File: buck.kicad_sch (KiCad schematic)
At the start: 24 parts, among them IC2 LV2862YDDCR, IC2 RT6285GSP

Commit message: Update footprints + pass DRC
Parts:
- L1: footprint Robomaster_ICs:MPLAL6060100 -> Robomaster_Passives:MPLAL6060100
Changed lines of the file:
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@@
       (effects (font (size 1.27 1.27)))
     )
-    (property "Footprint" "Robomaster_ICs:MPLAL6060100" (at 114.3 90.17 0)
+    (property "Footprint" "Robomaster_Passives:MPLAL6060100" (at 114.3 90.17 0)
       (effects (font (size 1.27 1.27)) hide)
     )

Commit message: Replace inductor with larger
Idk how much current it'll need + invalid inductor data for spreadsheet
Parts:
- L1: footprint Inductor_SMD:L_Murata_LQH2MCNxxxx02_2.0x1.6mm -> Robomaster_Passives:SRN3012BTA330M; Manufacturer_Name (none) -> Bourns; Manufacturer_Part_Number (none) -> SRN3012BTA-330M; Mouser Part Number (none) -> 652-SRN3012BTA-330M
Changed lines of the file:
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@@
       (effects (font (size 1.27 1.27)))
     )
-    (property "Footprint" "Inductor_SMD:L_Murata_LQH2MCNxxxx02_2.0x1.6mm" (at 139.7 130.81 0)
+    (property "Footprint" "Robomaster_Passives:SRN3012BTA330M" (at 139.7 130.81 0)
       (effects (font (size 1.27 1.27)) hide)
     )
-    (property "Datasheet" "https://www.we-online.com/components/products/datasheet/74404024330.pdf" (at 139.7 130.81 0)
+    (property "Datasheet" "https://www.mouser.com/datasheet/2/54/Bourns_08042023_SRN3012BTA_datasheet-3305898.pdf" (at 139.7 130.81 0)
       (effects (font (size 1.27 1.27)) hide)
     )
+    (property "Manufacturer_Name" "Bourns" (at 139.7 130.81 0)
+      (effects (font (size 1.27 1.27)) hide)
+    )
+    (property "Manufacturer_Part_Number" "SRN3012BTA-330M" (at 139.7 130.81 0)
+      (effects (font (size 1.27 1.27)) hide)
+    )
+    (property "Mouser Part Number" "652-SRN3012BTA-330M" (at 139.7 130.81 0)
+      (effects (font (size 1.27 1.27)) hide)
+    )

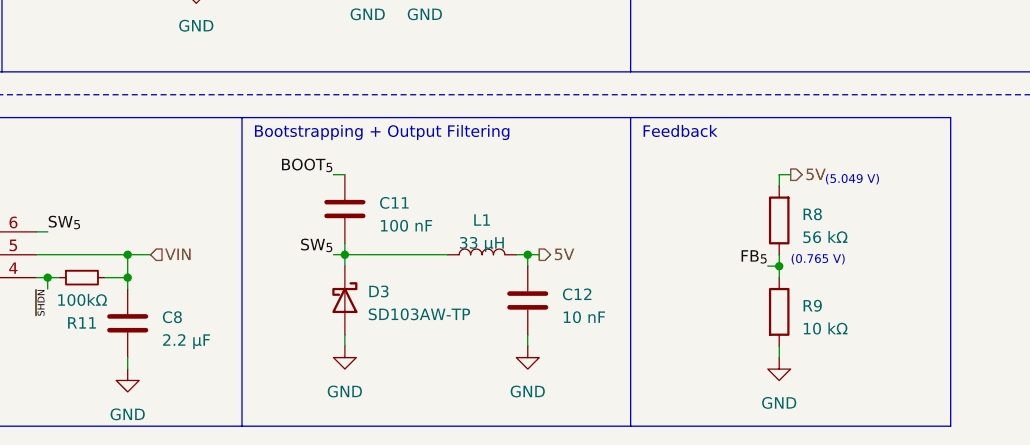
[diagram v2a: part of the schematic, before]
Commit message: Update and generate IBOM
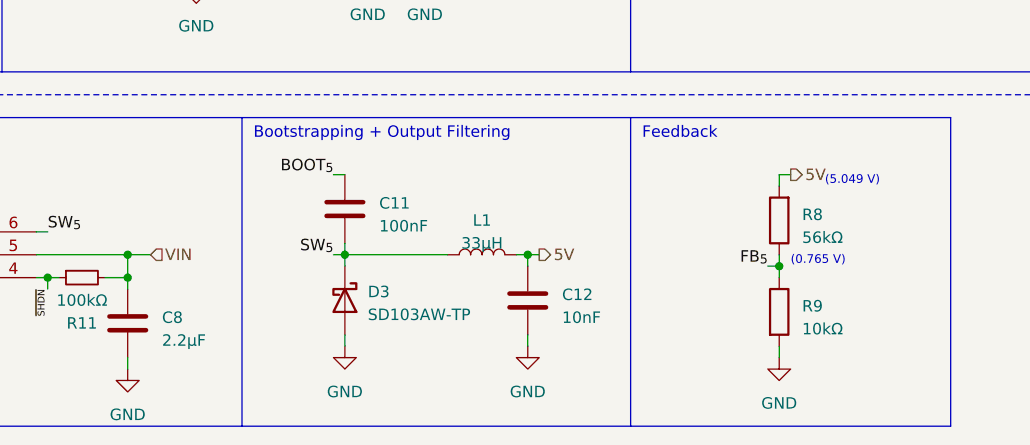
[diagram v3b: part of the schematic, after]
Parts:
- C1: Manufacturer_Part_Number (none) -> C0603C103J5RACAUTO; Mouser Part Number (none) -> 80-C0603C103J5RAUTO
- C11: value 100 nF -> 100nF; Manufacturer_Part_Number (none) -> CL10B104JB8NNNC; Mouser Part Number (none) -> 187-CL10B104JB8NNNC
- C12: value 10 nF -> 10nF; Manufacturer_Part_Number (none) -> C0603C103J5RACAUTO; Mouser Part Number (none) -> 80-C0603C103J5RAUTO
- C3: Manufacturer_Part_Number (none) -> CC0603FRNPO0BN820; Mouser Part Number (none) -> 603-CC0603FRNP0BN820
- C5, C6: Manufacturer_Part_Number (none) -> CL21A226MAYNNNE; Mouser Part Number (none) -> 187-CL21A226MAYNNNE
- C7, C8: Manufacturer_Part_Number (none) -> C1608X5R1E475K080AC; Mouser Part Number (none) -> 810-C1608X5R1E475K
- C8: value 2.2 μF -> 2.2μF; Manufacturer_Part_Number (none) -> GRM188R61E225KA2J; Mouser Part Number (none) -> 81-GRM188R61E225KA2J
- D3: Manufacturer_Part_Number (none) -> BAS321JX; Mouser Part Number (none) -> 771-BAS321JX
- D3: Manufacturer_Part_Number (none) -> SD103AW-TP; Mouser Part Number (none) -> 833-SD103AW-TP
- D4: Manufacturer_Part_Number (none) -> SR54F-AU_R2_000A1; Mouser Part Number (none) -> 241-SR54F-AUR1000A1
- L1: Manufacturer_Part_Number (none) -> MPL-AL6060-100; Mouser Part Number (none) -> 946-MPL-AL6060-100
- L1: value 33 μH -> 33μH
- R11, R3: Manufacturer_Part_Number (none) -> RT0603DRE07100KL; Mouser Part Number (none) -> 603-RT0603DRE07100KL
- R4: Manufacturer_Part_Number (none) -> RT0603DRE076K8L; Mouser Part Number (none) -> 603-RT0603DRE076K8L
- R8: value 56 kΩ -> 56kΩ; Manufacturer_Part_Number (none) -> RT0603DRD0756KL; Mouser Part Number (none) -> 603-RT0603DRD0756KL
- R9: value 10 kΩ -> 10kΩ; Manufacturer_Part_Number (none) -> RT0603DRE0710KL; Mouser Part Number (none) -> 603-RT0603DRE0710KL
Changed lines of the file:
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@@
+      (effects (font (size 1.27 1.27)) hide)
+    )
+    (property "Manufacturer_Part_Number" "C1608X5R1E475K080AC" (at 142.24 60.96 0)
+      (effects (font (size 1.27 1.27)) hide)
+    )
+    (property "Mouser Part Number" "810-C1608X5R1E475K" (at 142.24 60.96 0)
       (effects (font (size 1.27 1.27)) hide)
     )
@@
       (effects (font (size 1.27 1.27)) hide)
     )
+    (property "Manufacturer_Part_Number" "CC0603FRNPO0BN820" (at 110.49 55.88 0)
+      (effects (font (size 1.27 1.27)) hide)
+    )
+    (property "Mouser Part Number" "603-CC0603FRNP0BN820" (at 110.49 55.88 0)
+      (effects (font (size 1.27 1.27)) hide)
+    )
     (pin "1")
     (pin "2")
@@
     )
     (property "Datasheet" "~" (at 97.79 66.04 0)
+      (effects (font (size 1.27 1.27)) hide)
+    )
+    (property "Manufacturer_Part_Number" "RT0603DRE076K8L" (at 97.79 66.04 0)
+      (effects (font (size 1.27 1.27)) hide)
+    )
+    (property "Mouser Part Number" "603-RT0603DRE076K8L" (at 97.79 66.04 0)
       (effects (font (size 1.27 1.27)) hide)
     )
@@
       (effects (font (size 1.27 1.27)) hide)
     )
+    (property "Manufacturer_Part_Number" "SR54F-AU_R2_000A1" (at 107.95 95.25 0)
+      (effects (font (size 1.27 1.27)) hide)
+    )
+    (property "Mouser Part Number" "241-SR54F-AUR1000A1" (at 107.95 95.25 0)
+      (effects (font (size 1.27 1.27)) hide)
+    )
     (pin "1")
     (pin "2")
@@
     )
     (property "Datasheet" "https://www.mouser.com/datasheet/2/277/MPL_AL6060_100-2946374.pdf" (at 114.3 90.17 0)
+      (effects (font (size 1.27 1.27)) hide)
+    )
+    (property "Manufacturer_Part_Number" "MPL-AL6060-100" (at 114.3 90.17 0)
+      (effects (font (size 1.27 1.27)) hide)
+    )
+    (property "Mouser Part Number" "946-MPL-AL6060-100" (at 114.3 90.17 0)
       (effects (font (size 1.27 1.27)) hide)
     )
@@
       (effects (font (size 1.27 1.27)) hide)
     )
-    (property "Datasheet" "https://www.mouser.com/datasheet/2/447/KEM_C1002_X7R_SMD-3316098.pdf" (at 71.12 83.82 0)
+    (property "Datasheet" "~" (at 71.12 83.82 0)
+      (effects (font (size 1.27 1.27)) hide)
+    )
+    (property "Manufacturer_Part_Number" "C0603C103J5RACAUTO" (at 71.12 83.82 0)
+      (effects (font (size 1.27 1.27)) hide)
+    )
+    (property "Mouser Part Number" "80-C0603C103J5RAUTO" (at 71.12 83.82 0)
       (effects (font (size 1.27 1.27)) hide)
     )
@@
       (effects (font (size 1.27 1.27)) (justify right))
     )
-    (property "Value" "56 kΩ" (at 175.26 128.905 0)
+    (property "Value" "56kΩ" (at 175.26 128.905 0)
       (effects (font (size 1.27 1.27)) (justify right))
     )
@@
     )
     (property "Datasheet" "~" (at 172.72 127 0)
+      (effects (font (size 1.27 1.27)) hide)
+    )
+    (property "Manufacturer_Part_Number" "RT0603DRD0756KL" (at 172.72 127 0)
+      (effects (font (size 1.27 1.27)) hide)
+    )
+    (property "Mouser Part Number" "603-RT0603DRD0756KL" (at 172.72 127 0)
       (effects (font (size 1.27 1.27)) hide)
     )
@@
       (effects (font (size 1.27 1.27)) hide)
     )
+    (property "Manufacturer_Part_Number" "C1608X5R1E475K080AC" (at 135.89 60.96 0)
+      (effects (font (size 1.27 1.27)) hide)
+    )
+    (property "Mouser Part Number" "810-C1608X5R1E475K" (at 135.89 60.96 0)
+      (effects (font (size 1.27 1.27)) hide)
+    )
     (pin "1")
     (pin "2")
@@
       (effects (font (size 1.27 1.27)) (justify left))
     )
-    (property "Value" "10 nF" (at 148.59 137.795 0)
+    (property "Value" "10nF" (at 148.59 137.795 0)
       (effects (font (size 1.27 1.27)) (justify left))
     )
@@
     )
     (property "Datasheet" "~" (at 144.78 135.89 0)
+      (effects (font (size 1.27 1.27)) hide)
+    )
+    (property "Manufacturer_Part_Number" "C0603C103J5RACAUTO" (at 144.78 135.89 0)
+      (effects (font (size 1.27 1.27)) hide)
+    )
+    (property "Mouser Part Number" "80-C0603C103J5RAUTO" (at 144.78 135.89 0)
       (effects (font (size 1.27 1.27)) hide)
     )
@@
       (effects (font (size 1.27 1.27)) hide)
     )
+    (property "Manufacturer_Part_Number" "CL21A226MAYNNNE" (at 127 93.98 0)
+      (effects (font (size 1.27 1.27)) hide)
+    )
+    (property "Mouser Part Number" "187-CL21A226MAYNNNE" (at 127 93.98 0)
+      (effects (font (size 1.27 1.27)) hide)
+    )
     (pin "1")
     (pin "2")
@@
     )
     (property "Sim.Pins" "1=K 2=A" (at 67.31 78.74 0)
+      (effects (font (size 1.27 1.27)) hide)
+    )
+    (property "Manufacturer_Part_Number" "BAS321JX" (at 67.31 78.74 0)
+      (effects (font (size 1.27 1.27)) hide)
+    )
+    (property "Mouser Part Number" "771-BAS321JX" (at 67.31 78.74 0)
       (effects (font (size 1.27 1.27)) hide)
     )
@@
       (effects (font (size 1.27 1.27)) hide)
     )
+    (property "Manufacturer_Part_Number" "CL21A226MAYNNNE" (at 133.35 93.98 0)
+      (effects (font (size 1.27 1.27)) hide)
+    )
+    (property "Mouser Part Number" "187-CL21A226MAYNNNE" (at 133.35 93.98 0)
+      (effects (font (size 1.27 1.27)) hide)
+    )
     (pin "1")
     (pin "2")
@@
       (effects (font (size 1.27 1.27)) hide)
     )
+    (property "Manufacturer_Part_Number" "RT0603DRE07100KL" (at 97.79 55.88 0)
+      (effects (font (size 1.27 1.27)) hide)
+    )
+    (property "Mouser Part Number" "603-RT0603DRE07100KL" (at 97.79 55.88 0)
+      (effects (font (size 1.27 1.27)) hide)
+    )
     (pin "1")
     (pin "2")
@@
       (effects (font (size 1.27 1.27)) (justify left))
     )
-    (property "Value" "10 kΩ" (at 175.26 139.065 0)
+    (property "Value" "10kΩ" (at 175.26 139.065 0)
       (effects (font (size 1.27 1.27)) (justify left))
     )
@@
     )
     (property "Datasheet" "~" (at 172.72 137.16 0)
+      (effects (font (size 1.27 1.27)) hide)
+    )
+    (property "Manufacturer_Part_Number" "RT0603DRE0710KL" (at 172.72 137.16 0)
+      (effects (font (size 1.27 1.27)) hide)
+    )
+    (property "Mouser Part Number" "603-RT0603DRE0710KL" (at 172.72 137.16 0)
       (effects (font (size 1.27 1.27)) hide)
     )
@@
       (effects (font (size 1.27 1.27)))
     )
-    (property "Value" "33 μH" (at 139.7 129.54 90)
+    (property "Value" "33μH" (at 139.7 129.54 90)
       (effects (font (size 1.27 1.27)))
     )
@@
       (effects (font (size 1.27 1.27)) (justify left))
     )
-    (property "Value" "2.2 μF" (at 104.14 140.335 0)
+    (property "Value" "2.2μF" (at 104.14 140.335 0)
       (effects (font (size 1.27 1.27)) (justify left))
     )
@@
     )
     (property "Datasheet" "https://www.mouser.com/datasheet/2/585/MLCC-1837944.pdf" (at 100.33 138.43 0)
+      (effects (font (size 1.27 1.27)) hide)
+    )
+    (property "Manufacturer_Part_Number" "GRM188R61E225KA2J" (at 100.33 138.43 0)
+      (effects (font (size 1.27 1.27)) hide)
+    )
+    (property "Mouser Part Number" "81-GRM188R61E225KA2J" (at 100.33 138.43 0)
       (effects (font (size 1.27 1.27)) hide)
     )
@@
       (effects (font (size 1.27 1.27)) (justify left))
     )
-    (property "Value" "100 nF" (at 128.27 127.635 0)
+    (property "Value" "100nF" (at 128.27 127.635 0)
       (effects (font (size 1.27 1.27)) (justify left))
     )
@@
     )
     (property "Datasheet" "https://www.mouser.com/datasheet/2/585/MLCC-1837944.pdf" (at 124.46 125.73 0)
+      (effects (font (size 1.27 1.27)) hide)
+    )
+    (property "Manufacturer_Part_Number" "CL10B104JB8NNNC" (at 124.46 125.73 0)
+      (effects (font (size 1.27 1.27)) hide)
+    )
+    (property "Mouser Part Number" "187-CL10B104JB8NNNC" (at 124.46 125.73 0)
       (effects (font (size 1.27 1.27)) hide)
     )
@@
       (effects (font (size 1.27 1.27)) hide)
     )
+    (property "Manufacturer_Part_Number" "RT0603DRE07100KL" (at 95.25 133.35 0)
+      (effects (font (size 1.27 1.27)) hide)
+    )
+    (property "Mouser Part Number" "603-RT0603DRE07100KL" (at 95.25 133.35 0)
+      (effects (font (size 1.27 1.27)) hide)
+    )
     (pin "1")
     (pin "2")
@@
       (effects (font (size 1.27 1.27)) hide)
     )
+    (property "Manufacturer_Part_Number" "SD103AW-TP" (at 124.46 135.89 0)
+      (effects (font (size 1.27 1.27)) hide)
+    )
+    (property "Mouser Part Number" "833-SD103AW-TP" (at 124.46 135.89 0)
+      (effects (font (size 1.27 1.27)) hide)
+    )

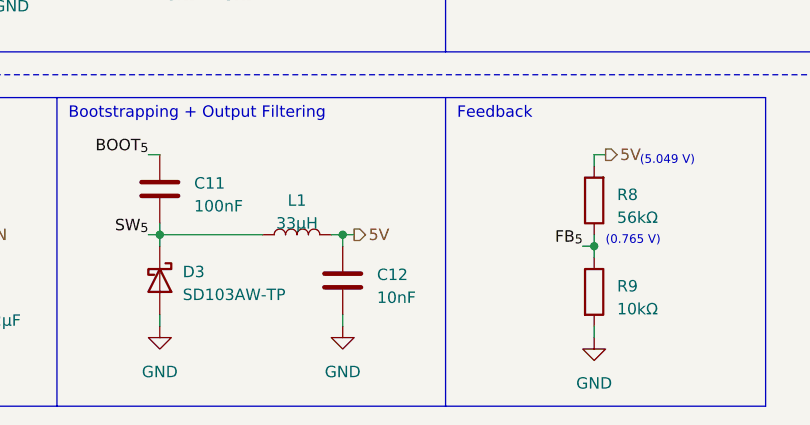
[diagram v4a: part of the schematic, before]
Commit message: added supercap connection
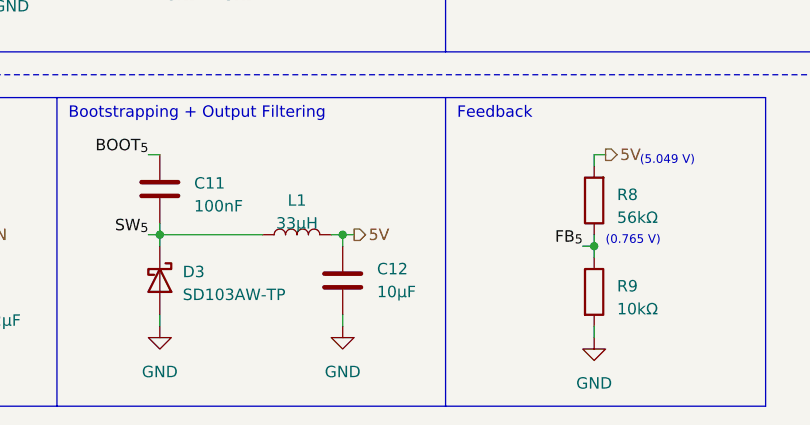
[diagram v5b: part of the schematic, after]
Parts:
- C12: value 10nF -> 10μF; Mouser Part Number 80-C0603C103J5RAUTO -> 187-CL10A106KP8NNWC
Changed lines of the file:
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@@
 		(fields_autoplaced yes)
 		(property "Reference" "C12"
-			(at 148.59 135.255 0)
+			(at 148.59 134.6199 0)
 			(effects
 				(font
@@
 			)
 		)
-		(property "Value" "10nF"
-			(at 148.59 137.795 0)
+		(property "Value" "10μF"
+			(at 148.59 137.1599 0)
 			(effects
 				(font
@@
 			)
 		)
-		(property "Mouser Part Number" "80-C0603C103J5RAUTO"
+		(property "Mouser Part Number" "187-CL10A106KP8NNWC"
 			(at 144.78 135.89 0)
 			(effects

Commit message: Prepped Chassis for final review
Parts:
- removed C1: 10nF, Capacitor_SMD:C_0603_1608Metric_Pad1.08x0.95mm_HandSolder, symbol Device:C
- removed C11: 100nF, Capacitor_SMD:C_0603_1608Metric_Pad1.08x0.95mm_HandSolder, symbol Device:C
- removed C12: 10μF, Capacitor_SMD:C_0603_1608Metric_Pad1.08x0.95mm_HandSolder, symbol Device:C
- removed C8: 2.2μF, Capacitor_SMD:C_0603_1608Metric_Pad1.08x0.95mm_HandSolder, symbol Device:C
- removed D3: BAS321J, Diode_SMD:D_SOD-323F, symbol Device:D
- removed D3: SD103AW-TP, Diode_SMD:D_SOD-123, symbol Device:D_Schottky
- removed IC2: LV2862YDDCR, Robomaster_ICs:SOT95P280X110-6N, symbol _LHRE_ICs:LV2862YDDCR
- removed L1: 33μH, Robomaster_Passives:SRN3012BTA330M, symbol Device:L
- removed R11: 100kΩ, Resistor_SMD:R_0603_1608Metric_Pad0.98x0.95mm_HandSolder, symbol Device:R_Small
- removed R8: 56kΩ, Resistor_SMD:R_0603_1608Metric_Pad0.98x0.95mm_HandSolder, symbol Device:R
- removed R9: 10kΩ, Resistor_SMD:R_0603_1608Metric_Pad0.98x0.95mm_HandSolder, symbol Device:R
- removed TP5: TestPoint, TestPoint:TestPoint_Pad_2.0x2.0mm, symbol Connector:TestPoint
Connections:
- net BOOT_{19}: no longer names the net of IC2.1 (BOOT)
- no-connect marks 3 -> 4
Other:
- note added: ""GND" here provided by MINIPC"
- note removed: "(0.765 V)"
- note removed: "(5.049 V)"
- note removed: "5V"
- note removed: "Bootstraping (diode + cap)"
- note removed: "Bootstrapping + Output Filtering"
- note removed: "Buck Converter + Input Filtering"
- note removed: "Feedback"
- moved on the sheet: C3, C5, C6, C7, C8, D4, IC2, L1, R3, R4, TP3, TP4
